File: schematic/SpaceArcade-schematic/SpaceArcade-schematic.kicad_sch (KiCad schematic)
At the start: 2 parts

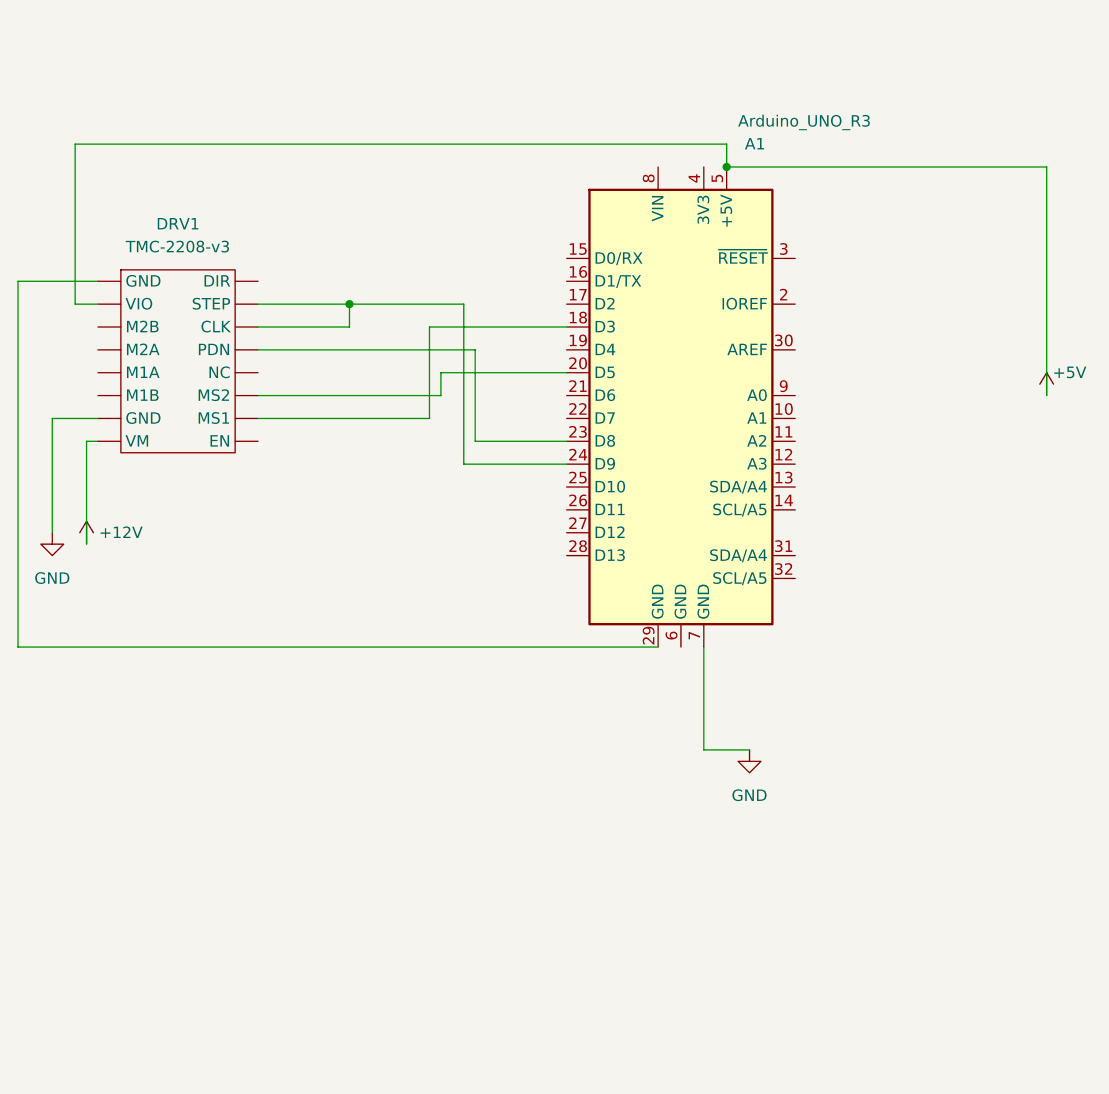
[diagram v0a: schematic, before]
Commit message: Updating and adding custom components
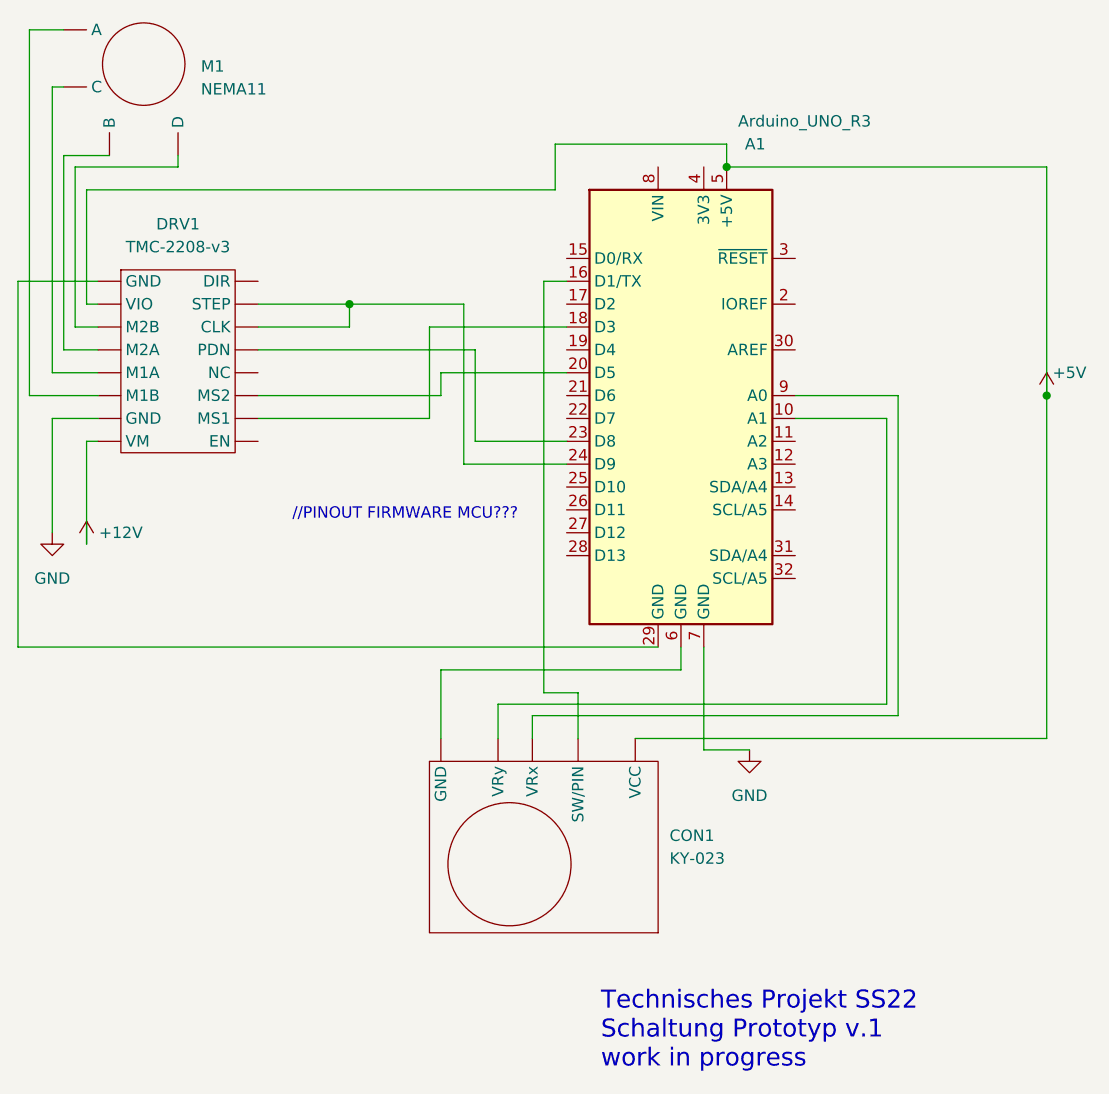
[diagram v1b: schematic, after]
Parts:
- added CON1: KY-023, symbol FunDuino:KY-023
- added M1: NEMA11, symbol NEMA-motor:NEMA11
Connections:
- net +5V: now also CON1. (VRy)
- net at A1.10 (A1): now also CON1. (VRy)
- net at A1.16 (D1/TX): now also CON1. (VRy)
- net at A1.6 (GND): now also CON1. (VRy)
- net at A1.9 (A0): now also CON1. (VRy)
- new net: DRV1. (VM), M1. (D) (x4)
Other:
- note added: "//PINOUT FIRMWARE MCU???"
- note added: "Technisches Projekt SS22 Schaltung Prototyp v.1 work in progress"
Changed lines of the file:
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@@
 (kicad_sch (version 20211123) (generator eeschema)
   (paper "A4")
-  (junction (at 194.31 78.74) (diameter 0) (color 0 0 0 0)
+  (junction (at 194.31 78.74) (diameter 0) (color 255 0 0 1)
   )
   (junction (at 152.4 93.98) (diameter 0) (color 255 0 255 1)
   )
+  (junction (at 229.87 104.14) (diameter 0) (color 0 0 0 0)
+  )
+  (wire (pts (xy 116.84 104.14) (xy 124.46 104.14))
+    (stroke (width 0) (type default) (color 255 153 0 1))
+  )
+  (wire (pts (xy 177.8 137.16) (xy 173.99 137.16))
+    (stroke (width 0) (type default) (color 255 255 0 1))
+  )
+  (wire (pts (xy 120.65 77.47) (xy 125.73 77.47))
+    (stroke (width 0) (type default) (color 0 0 0 0))
+  )
+  (wire (pts (xy 184.15 142.24) (xy 229.87 142.24))
+    (stroke (width 0) (type default) (color 255 0 0 1))
+  )
   (wire (pts (xy 191.77 143.51) (xy 196.85 143.51))
     (stroke (width 0) (type default) (color 0 0 0 1))
@@
   (wire (pts (xy 142.24 99.06) (xy 166.37 99.06))
     (stroke (width 0) (type default) (color 0 255 255 1))
+  )
+  (wire (pts (xy 123.19 81.28) (xy 175.26 81.28))
+    (stroke (width 0) (type default) (color 255 0 0 1))
+  )
+  (wire (pts (xy 212.09 106.68) (xy 201.93 106.68))
+    (stroke (width 0) (type default) (color 132 0 132 1))
   )
   (wire (pts (xy 142.24 104.14) (xy 162.56 104.14))
     (stroke (width 0) (type default) (color 0 0 255 1))
   )
-  (wire (pts (xy 121.92 76.2) (xy 194.31 76.2))
-    (stroke (width 0) (type default) (color 255 0 0 1))
+  (wire (pts (xy 120.65 63.5) (xy 116.84 63.5))
+    (stroke (width 0) (type default) (color 255 153 0 1))
+  )
+  (wire (pts (xy 119.38 101.6) (xy 119.38 69.85))
+    (stroke (width 0) (type default) (color 0 132 132 1))
+  )
+  (wire (pts (xy 213.36 104.14) (xy 201.93 104.14))
+    (stroke (width 0) (type default) (color 0 255 255 1))
   )
   (wire (pts (xy 162.56 104.14) (xy 162.56 101.6))
@@
     (stroke (width 0) (type default) (color 255 0 255 1))
   )
+  (wire (pts (xy 213.36 139.7) (xy 213.36 104.14))
+    (stroke (width 0) (type default) (color 0 255 255 1))
+  )
   (wire (pts (xy 165.1 93.98) (xy 152.4 93.98))
     (stroke (width 0) (type default) (color 255 0 255 1))
@@
     (stroke (width 0) (type default) (color 255 0 0 1))
   )
+  (wire (pts (xy 177.8 142.24) (xy 177.8 137.16))
+    (stroke (width 0) (type default) (color 255 255 0 1))
+  )
   (wire (pts (xy 229.87 104.14) (xy 229.87 78.74))
     (stroke (width 0) (type default) (color 255 0 0 1))
   )
+  (wire (pts (xy 229.87 142.24) (xy 229.87 104.14))
+    (stroke (width 0) (type default) (color 255 0 0 1))
+  )
   (wire (pts (xy 115.57 132.08) (xy 186.69 132.08))
     (stroke (width 0) (type default) (color 0 0 0 1))
   )
+  (wire (pts (xy 168.91 142.24) (xy 168.91 138.43))
+    (stroke (width 0) (type default) (color 132 0 132 1))
+  )
+  (wire (pts (xy 175.26 76.2) (xy 194.31 76.2))
+    (stroke (width 0) (type default) (color 255 0 0 1))
+  )
   (wire (pts (xy 115.57 91.44) (xy 124.46 91.44))
     (stroke (width 0) (type default) (color 0 0 0 1))
@@
     (stroke (width 0) (type default) (color 255 0 255 1))
   )
+  (wire (pts (xy 162.56 134.62) (xy 189.23 134.62))
+    (stroke (width 0) (type default) (color 0 0 0 1))
+  )
+  (wire (pts (xy 172.72 139.7) (xy 213.36 139.7))
+    (stroke (width 0) (type default) (color 0 255 255 1))
+  )
   (wire (pts (xy 119.38 119.38) (xy 119.38 106.68))
     (stroke (width 0) (type default) (color 0 0 0 1))
   )
+  (wire (pts (xy 124.46 99.06) (xy 120.65 99.06))
+    (stroke (width 0) (type default) (color 0 0 0 0))
+  )
+  (wire (pts (xy 124.46 101.6) (xy 119.38 101.6))
+    (stroke (width 0) (type default) (color 0 132 132 1))
+  )
   (wire (pts (xy 229.87 78.74) (xy 194.31 78.74))
     (stroke (width 0) (type default) (color 255 0 0 1))
   )
+  (wire (pts (xy 212.09 138.43) (xy 212.09 106.68))
+    (stroke (width 0) (type default) (color 132 0 132 1))
+  )
   (wire (pts (xy 119.38 106.68) (xy 124.46 106.68))
     (stroke (width 0) (type default) (color 0 0 0 1))
@@
   (wire (pts (xy 166.37 109.22) (xy 176.53 109.22))
     (stroke (width 0) (type default) (color 0 255 255 1))
+  )
+  (wire (pts (xy 120.65 77.47) (xy 120.65 99.06))
+    (stroke (width 0) (type default) (color 0 0 0 0))
   )
   (wire (pts (xy 161.29 96.52) (xy 176.53 96.52))
     (stroke (width 0) (type default) (color 0 255 0 1))
   )
-  (wire (pts (xy 124.46 93.98) (xy 121.92 93.98))
-    (stroke (width 0) (type default) (color 255 0 0 1))
-  )
   (wire (pts (xy 142.24 106.68) (xy 161.29 106.68))
     (stroke (width 0) (type default) (color 0 255 0 1))
@@
     (stroke (width 0) (type default) (color 0 255 0 1))
   )
+  (wire (pts (xy 121.92 96.52) (xy 121.92 78.74))
+    (stroke (width 0) (type default) (color 72 72 0 1))
+  )
+  (wire (pts (xy 189.23 134.62) (xy 189.23 132.08))
+    (stroke (width 0) (type default) (color 0 0 0 1))
+  )
   (wire (pts (xy 115.57 91.44) (xy 115.57 132.08))
     (stroke (width 0) (type default) (color 0 0 0 1))
   )
+  (wire (pts (xy 173.99 91.44) (xy 176.53 91.44))
+    (stroke (width 0) (type default) (color 255 255 0 1))
+  )
   (wire (pts (xy 191.77 132.08) (xy 191.77 143.51))
     (stroke (width 0) (type default) (color 0 0 0 1))
@@
     (stroke (width 0) (type default) (color 255 0 255 1))
   )
+  (wire (pts (xy 175.26 81.28) (xy 175.26 76.2))
+    (stroke (width 0) (type default) (color 255 0 0 1))
+  )
+  (wire (pts (xy 133.35 78.74) (xy 133.35 77.47))
+    (stroke (width 0) (type default) (color 72 72 0 1))
+  )
+  (wire (pts (xy 168.91 138.43) (xy 212.09 138.43))
+    (stroke (width 0) (type default) (color 132 0 132 1))
+  )
   (wire (pts (xy 123.19 120.65) (xy 123.19 109.22))
     (stroke (width 0) (type default) (color 255 0 0 1))
   )
+  (wire (pts (xy 123.19 81.28) (xy 123.19 93.98))
+    (stroke (width 0) (type default) (color 255 0 0 1))
+  )
   (wire (pts (xy 152.4 96.52) (xy 152.4 93.98))
     (stroke (width 0) (type default) (color 255 0 255 1))
   )
-  (wire (pts (xy 121.92 93.98) (xy 121.92 76.2))
-    (stroke (width 0) (type default) (color 255 0 0 1))
+  (wire (pts (xy 124.46 93.98) (xy 123.19 93.98))
+    (stroke (width 0) (type default) (color 255 0 0 1))
+  )
+  (wire (pts (xy 124.46 96.52) (xy 121.92 96.52))
+    (stroke (width 0) (type default) (color 72 72 0 1))
+  )
+  (wire (pts (xy 162.56 142.24) (xy 162.56 134.62))
+    (stroke (width 0) (type default) (color 0 0 0 1))
+  )
+  (wire (pts (xy 121.92 78.74) (xy 133.35 78.74))
+    (stroke (width 0) (type default) (color 72 72 0 1))
+  )
+  (wire (pts (xy 116.84 63.5) (xy 116.84 104.14))
+    (stroke (width 0) (type default) (color 255 153 0 1))
   )
   (wire (pts (xy 194.31 76.2) (xy 194.31 78.74))
     (stroke (width 0) (type default) (color 255 0 0 1))
+  )
+  (wire (pts (xy 172.72 142.24) (xy 172.72 139.7))
+    (stroke (width 0) (type default) (color 0 255 255 1))
+  )
+  (wire (pts (xy 119.38 69.85) (xy 120.65 69.85))
+    (stroke (width 0) (type default) (color 0 132 132 1))
+  )
+  (wire (pts (xy 173.99 137.16) (xy 173.99 91.44))
+    (stroke (width 0) (type default) (color 255 255 0 1))
+  )
+  (text "//PINOUT FIRMWARE MCU???" (at 146.05 118.11 0)
+    (effects (font (size 1.27 1.27)) (justify left bottom))
+  )
+  (text "Technisches Projekt SS22\nSchaltung Prototyp v.1\nwork in progress"
+    (at 180.34 179.07 0)
+    (effects (font (size 2 2)) (justify left bottom))
   )
   (symbol (lib_id "power:GND") (at 196.85 143.51 0) (unit 1)
@@
     (pin "1")
   )
+  (symbol (lib_id "NEMA-motor:NEMA11") (at 129.54 62.23 0) (unit 1)
+    (in_bom yes) (on_board yes) (fields_autoplaced)
+    (property "Reference" "M1" (id 0) (at 135.89 67.5603 0)
+      (effects (font (size 1.27 1.27)) (justify left))
+    )
+    (property "Value" "NEMA11" (id 1) (at 135.89 70.1003 0)
+      (effects (font (size 1.27 1.27)) (justify left))
+    )
+    (property "Footprint" "" (id 2) (at 129.54 62.23 0)
+      (effects (font (size 1.27 1.27)) hide)
+    )
+    (property "Datasheet" "" (id 3) (at 129.54 62.23 0)
+      (effects (font (size 1.27 1.27)) hide)
+    )
+    (pin "")
+    (pin "")
+    (pin "")
+    (pin "")
+  )
+  (symbol (lib_id "FunDuino:KY-023") (at 182.88 166.37 180) (unit 1)
+    (in_bom yes) (on_board yes) (fields_autoplaced)
+    (property "Reference" "CON1" (id 0) (at 187.96 153.0349 0)
+      (effects (font (size 1.27 1.27)) (justify right))
+    )
+    (property "Value" "KY-023" (id 1) (at 187.96 155.5749 0)
+      (effects (font (size 1.27 1.27)) (justify right))
+    )
+    (property "Footprint" "" (id 2) (at 182.88 166.37 0)
+      (effects (font (size 1.27 1.27)) hide)
+    )
+    (property "Datasheet" "" (id 3) (at 182.88 166.37 0)
+      (effects (font (size 1.27 1.27)) hide)
+    )
+    (pin "")
+    (pin "")
+    (pin "")
+    (pin "")
+    (pin "")
+  )
   (symbol (lib_id "power:+12V") (at 123.19 120.65 0) (unit 1)
     (in_bom yes) (on_board yes)
@@
       (reference "A1") (unit 1) (value "Arduino_UNO_R3") (footprint "Module:Arduino_UNO_R3")
     )
+    (path "/c58d4580-3cf0-43ae-aee8-92e1876c0e3e"
+      (reference "CON1") (unit 1) (value "KY-023") (footprint "")
+    )
     (path "/95578bbc-91c1-4fbb-b286-5c7e6bfb0f4c"
       (reference "DRV1") (unit 1) (value "TMC-2208-v3") (footprint "")
     )
-  )
+    (path "/c2cbae8f-edb4-4d3c-ba67-90e91f7d850a"
+      (reference "M1") (unit 1) (value "NEMA11") (footprint "")
+    )
+  )
